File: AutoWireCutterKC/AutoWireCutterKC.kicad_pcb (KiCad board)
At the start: 2 copper layers, 37.3 x 41.7 mm, 20 parts, among them J1 LCD I/O, J2 ISP, J8 Barrel_Jack, J9 Stepper, M1 Conn_01x01_Male, M2 Conn_01x01_Male, M3 Conn_01x01_Male, U1 ATMEGA328P-AU, U2 MCP1700_SOT23, U3 LT1129-5.0_SOT223

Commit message: Schematic Rev B
Changed footprint and silk screen issues
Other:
- board text added: "Rev B"
- board text removed: "Rev A"
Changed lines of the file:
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@@
   (layers
     (0 F.Cu signal)
-    (31 B.Cu signal hide)
+    (31 B.Cu signal)
     (32 B.Adhes user hide)
     (33 F.Adhes user hide)
     (34 B.Paste user hide)
     (35 F.Paste user hide)
-    (36 B.SilkS user hide)
+    (36 B.SilkS user)
     (37 F.SilkS user)
     (38 B.Mask user hide)
     (39 F.Mask user hide)
-    (44 Edge.Cuts user hide)
-    (46 B.CrtYd user)
-    (47 F.CrtYd user)
-    (48 B.Fab user)
-    (49 F.Fab user)
+    (44 Edge.Cuts user)
+    (46 B.CrtYd user hide)
+    (47 F.CrtYd user hide)
+    (48 B.Fab user hide)
+    (49 F.Fab user hide)
   )
   (setup
@@
     (tags "capacitor 0805")
     (attr smd)
-    (fp_text reference C3 (at 0 1.75) (layer B.SilkS)
+    (fp_text reference C3 (at 0 -1.778) (layer B.SilkS)
       (effects (font (size 1 1) (thickness 0.15)) (justify mirror))
     )
@@
     (tags "capacitor tantalum smd")
     (attr smd)
-    (fp_text reference C6 (at -5.08 0) (layer B.SilkS)
+    (fp_text reference C6 (at -5.334 0.508) (layer B.SilkS)
       (effects (font (size 1 1) (thickness 0.15)) (justify mirror))
     )
@@
     (tags "QFP 0.8")
     (attr smd)
-    (fp_text reference U1 (at 0 6.096) (layer B.SilkS)
+    (fp_text reference U1 (at -4.826 -4.572) (layer B.SilkS)
       (effects (font (size 1 1) (thickness 0.15)) (justify mirror))
     )
@@
     (tags SOT-23)
     (attr smd)
-    (fp_text reference U2 (at -2.54 -1.905 90) (layer B.SilkS)
+    (fp_text reference U2 (at -0.254 -2.54 90) (layer B.SilkS)
       (effects (font (size 1 1) (thickness 0.15)) (justify mirror))
     )
@@
     (tags "CMS SOT")
     (attr smd)
-    (fp_text reference U3 (at -5.715 3.175 180) (layer B.SilkS)
+    (fp_text reference U3 (at 1.524 -4.572 180) (layer B.SilkS)
       (effects (font (size 1 1) (thickness 0.15)) (justify mirror))
     )
@@
     (tags "connector jst ph")
     (attr smd)
-    (fp_text reference J9 (at -5.08 -2.54 360) (layer B.SilkS)
+    (fp_text reference J9 (at -7.874 0.508 360) (layer B.SilkS)
       (effects (font (size 1 1) (thickness 0.15)) (justify mirror))
     )
@@
     (pad 4 smd rect (at 3 -1.125 90) (size 1 5.5) (layers B.Cu B.Paste B.Mask)
       (net 8 "Net-(A1-Pad6)"))
-    (pad "" smd rect (at -5.4 1.125 90) (size 1.6 3) (layers B.Cu B.Paste B.Mask))
-    (pad "" smd rect (at 5.4 1.125 90) (size 1.6 3) (layers B.Cu B.Paste B.Mask))
+    (pad "" smd rect (at -5.588 2.54 90) (size 1.6 3) (layers B.Cu B.Paste B.Mask))
+    (pad "" smd rect (at 5.588 2.54 90) (size 1.6 3) (layers B.Cu B.Paste B.Mask))
     (model ${KISYS3DMOD}/Connectors_JST.3dshapes/JST_PH_B4B-PH-SM4-TB_04x2.00mm_Straight.wrl
       (at (xyz 0 0 0))
@@
   (gr_line (start 171.958 118.11) (end 171.958 79.756) (angle 90) (layer Edge.Cuts) (width 0.15))
   (gr_line (start 136.144 119.888) (end 170.18 119.888) (angle 90) (layer Edge.Cuts) (width 0.15))
-  (gr_text "Rev A" (at 149.86 108.204) (layer F.SilkS)
+  (gr_text "Rev B" (at 149.86 108.204) (layer F.SilkS)
     (effects (font (size 1.5 1.5) (thickness 0.2)))
   )

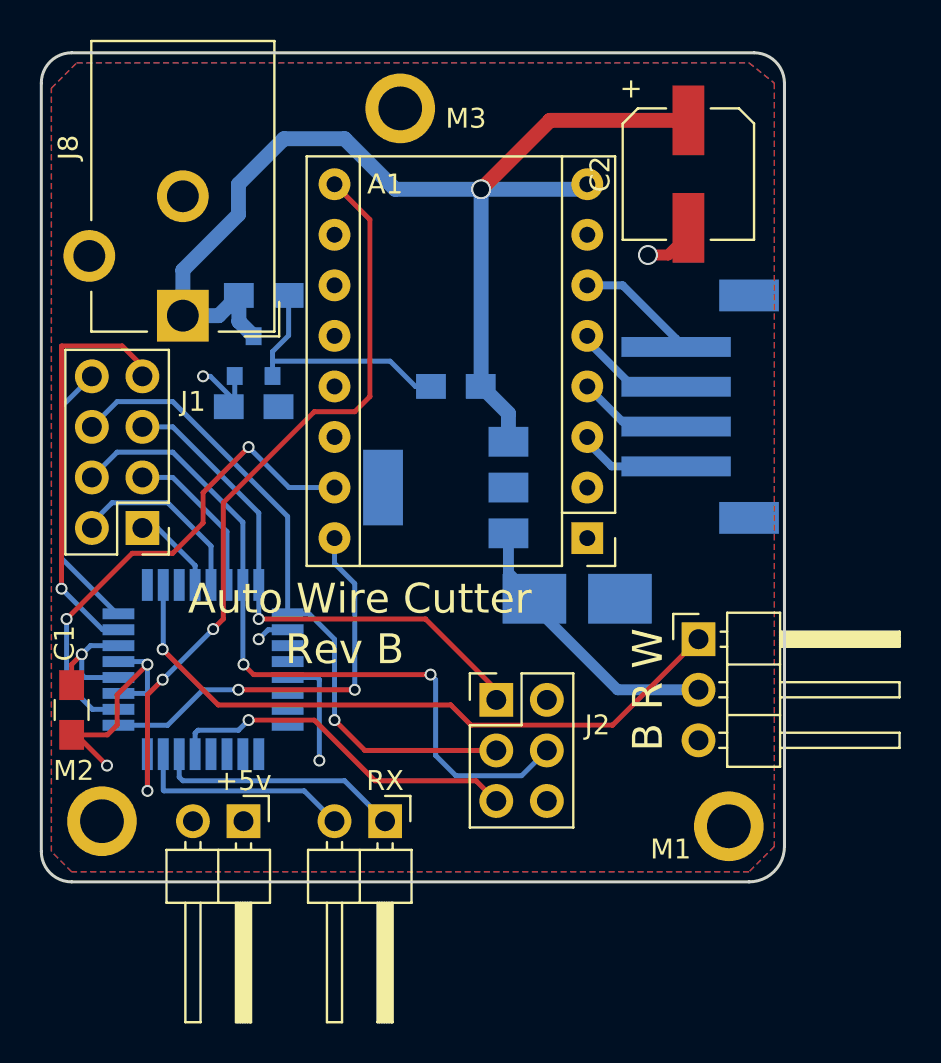
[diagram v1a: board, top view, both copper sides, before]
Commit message: Schematic Rev B
Moved silk screen, motor con through holes widened, motor connector fit on top.
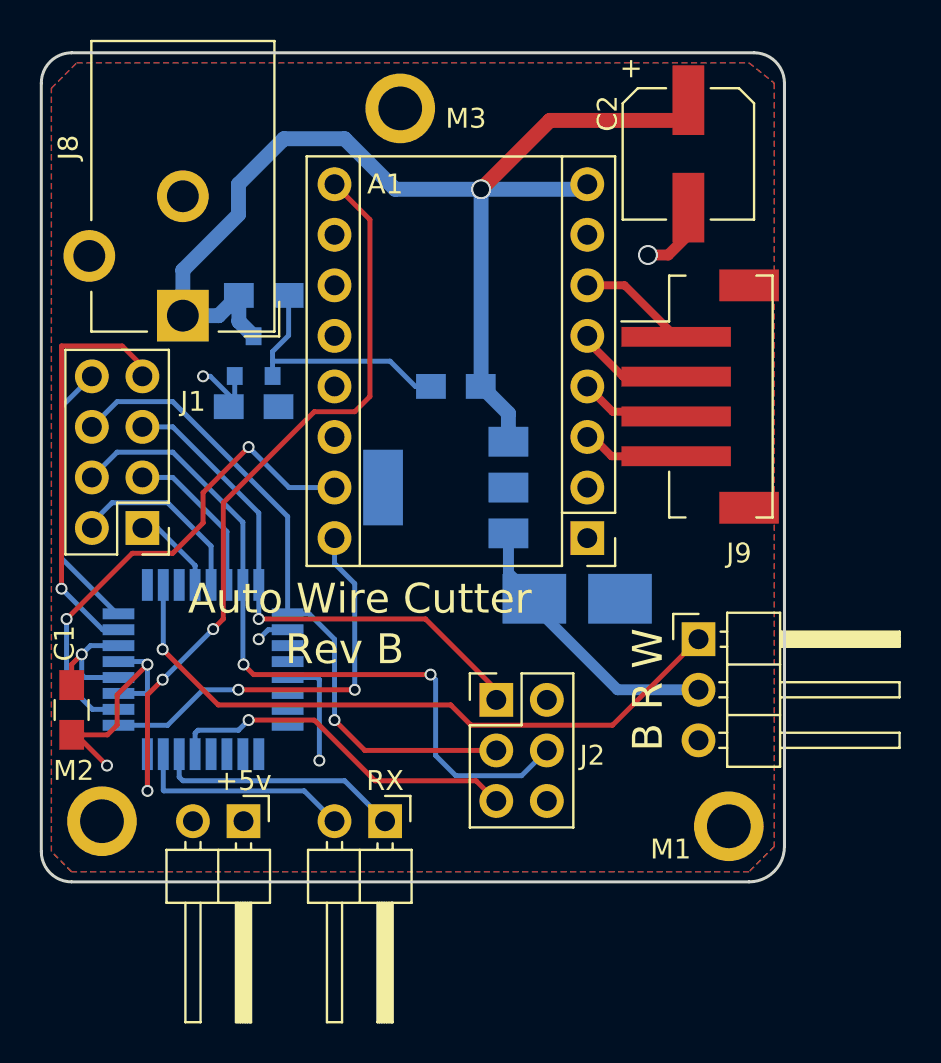
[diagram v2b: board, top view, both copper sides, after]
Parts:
- J9: moved to F.Cu
- moved C2 1.02 mm to (167.1, 83.3)
- moved J9 0.51 mm to (167.6, 95.5), turned to 270 degrees
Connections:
- J9 pad 1: Net-(A1-Pad3) -> Net-(A1-Pad6)
- J9 pad 2: Net-(A1-Pad4) -> Net-(A1-Pad5)
- J9 pad 3: Net-(A1-Pad5) -> Net-(A1-Pad4)
- J9 pad 4: Net-(A1-Pad6) -> Net-(A1-Pad3)
